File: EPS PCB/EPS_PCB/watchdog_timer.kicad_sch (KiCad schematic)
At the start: 5 parts, among them U1 TPS3431SDRBR

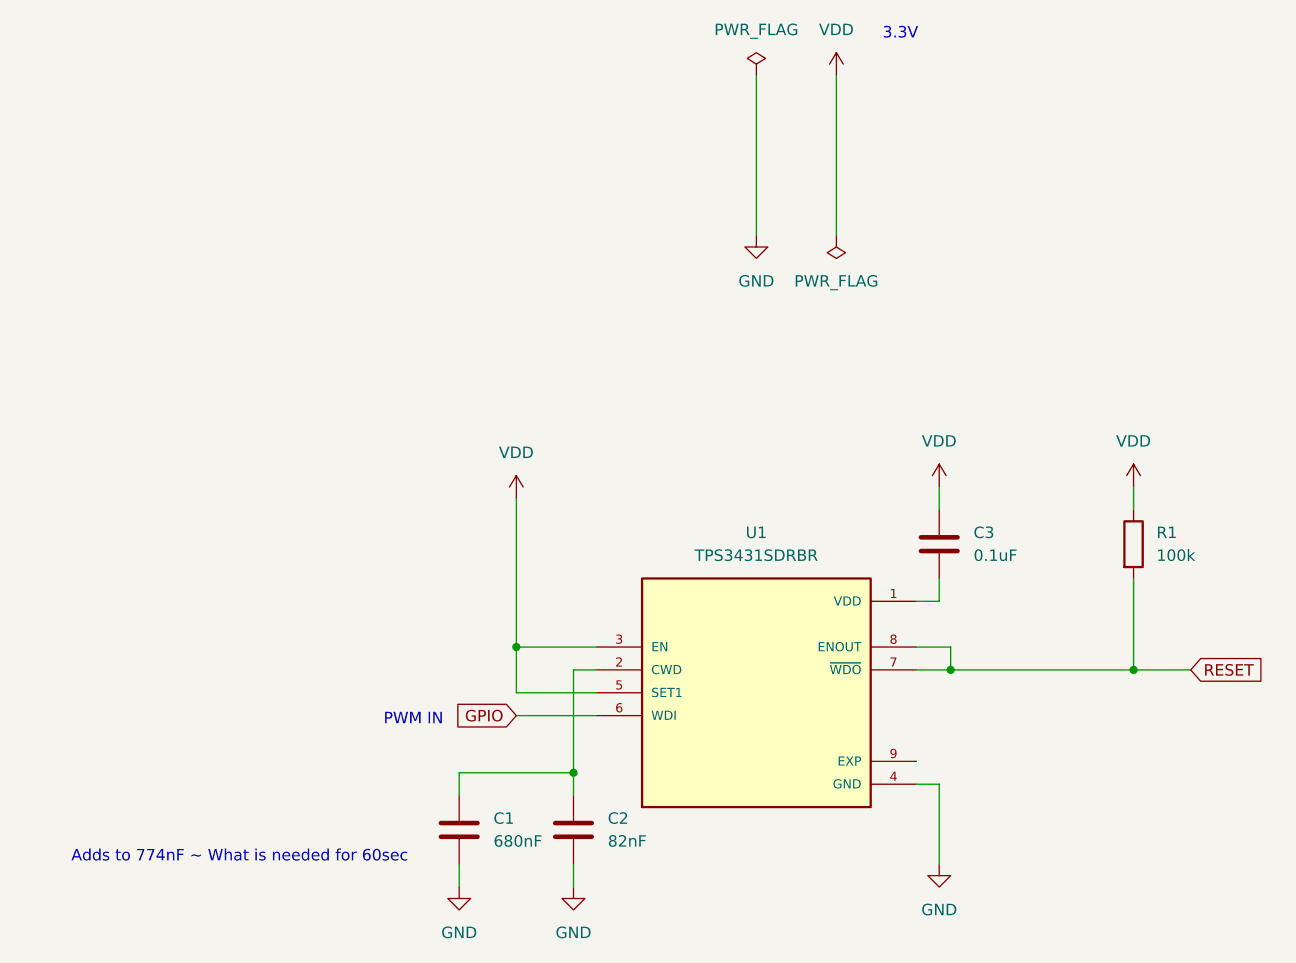
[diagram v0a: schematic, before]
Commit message: EPS PCB Added
- Added Heirarchal Project for the Main PDS Board
- Added PCI-104 Template PCB
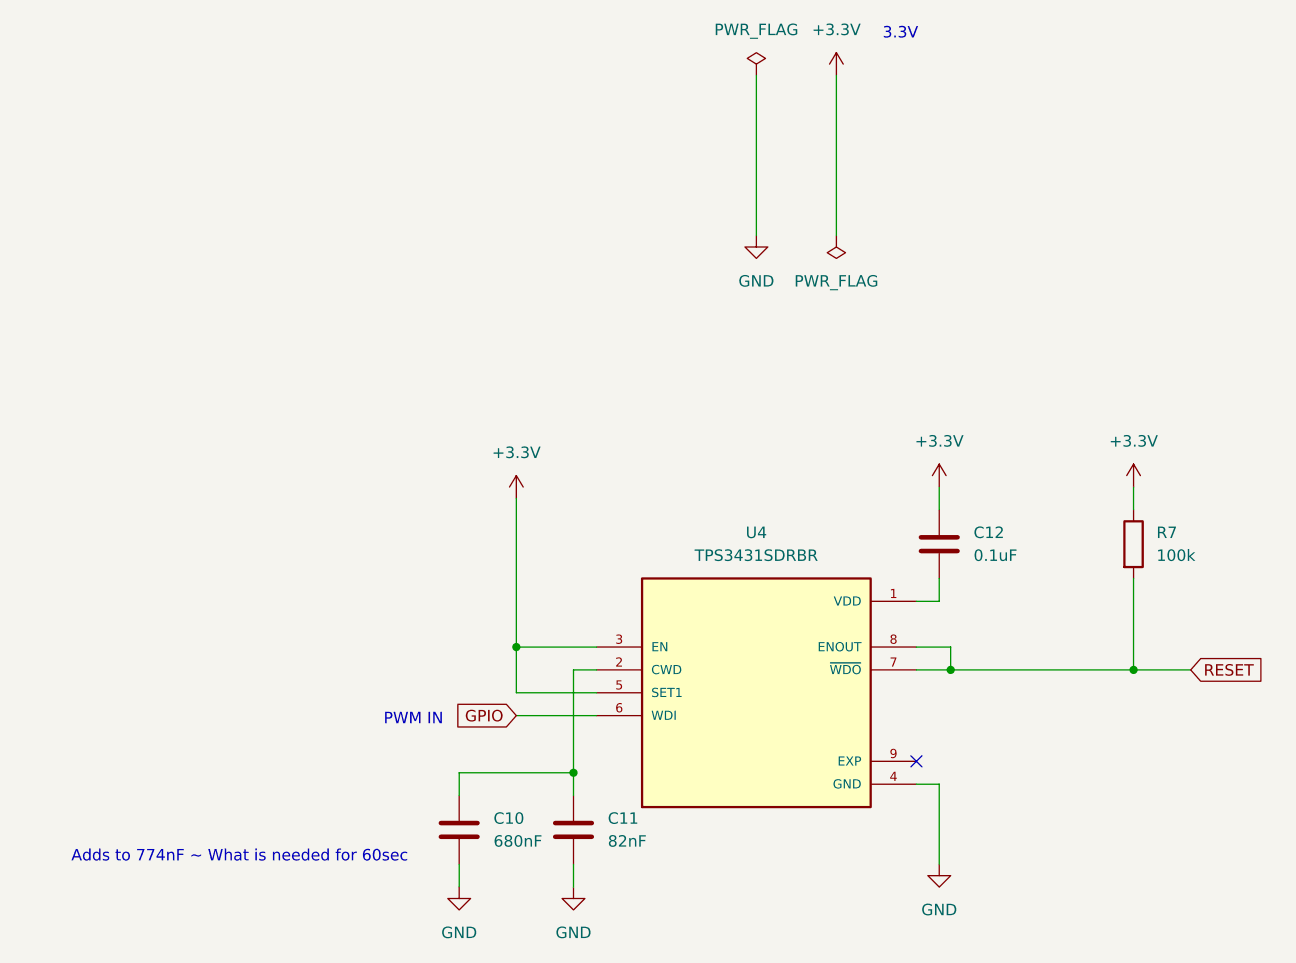
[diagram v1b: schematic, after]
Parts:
- C10: renamed from C1; footprint (none) -> Capacitor_SMD:C_1206_3216Metric
- C11: renamed from C2; footprint (none) -> Capacitor_SMD:C_1206_3216Metric
- C12: renamed from C3; footprint (none) -> Capacitor_SMD:C_0603_1608Metric
- R7: renamed from R1; footprint (none) -> Resistor_SMD:R_1206_3216Metric
- U4: renamed from U1; footprint TPS3431SDRBR:IC_TPS3431SDRBR -> Footprints:IC_TPS3431SDRBR
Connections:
- net VDD renamed +3.3V
- no-connect marks 0 -> 1

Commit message: PDR Update
Added Current Measurement, Hysteresis, EFuses
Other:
- company: (none) -> UW Huskysat
- title: (none) -> Watchdog Timeer Circuit
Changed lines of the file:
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@@
 	(generator_version "9.0")
 	(paper "A4")
+	(title_block
+		(title "Watchdog Timeer Circuit")
+		(date "2025-11-20")
+		(rev "1.0")
+		(company "UW Huskysat")
+		(comment 1 "Chase")
+	)
 	(text "PWM IN"
 		(exclude_from_sim no)
